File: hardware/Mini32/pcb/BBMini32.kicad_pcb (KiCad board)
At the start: 2 copper layers, 100 x 65 mm, 40 parts, among them J1 POWER, Q1 S8550, Q2 S8050, SW1 SW_Push, SW2 SW_Push, U1 ESP-32_NodeMCU, U2 74HC595, U3 HD44780, U4 MCP3208

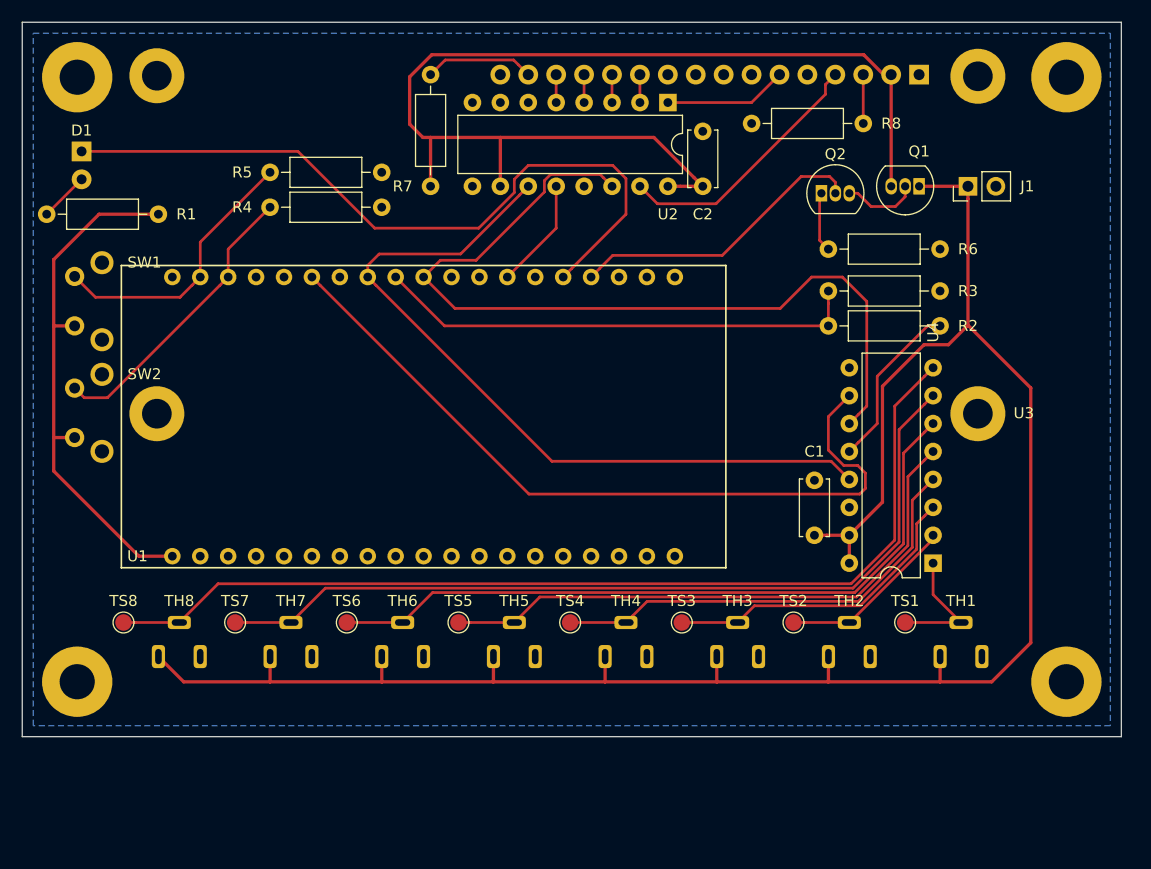
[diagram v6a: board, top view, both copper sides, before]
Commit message: feat: Use transistor to control display
resize and redo PCB

Issue #47
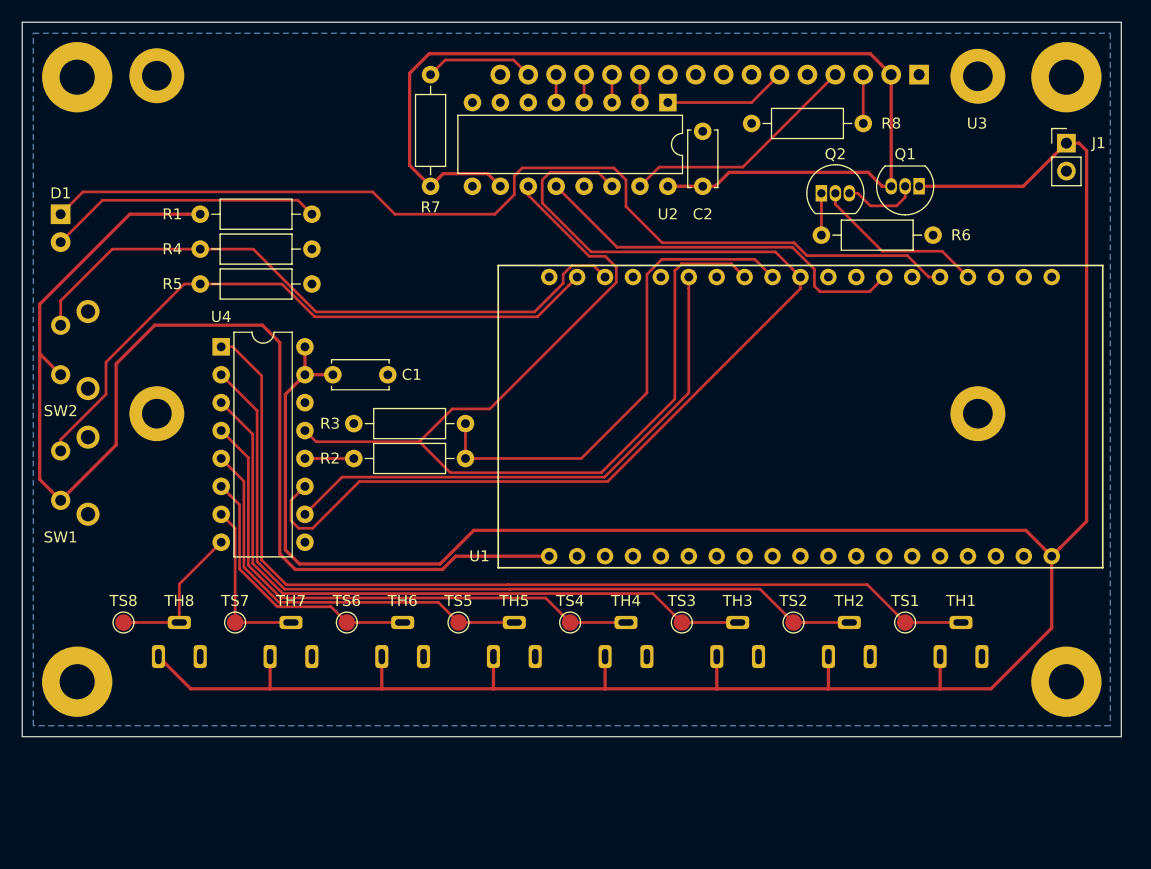
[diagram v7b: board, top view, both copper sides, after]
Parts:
- moved U4 67.7 mm to (38.1, 49.5), turned to 0 degrees
- moved R2 54.7 mm to (50.2, 59.7), turned to 0 degrees
- moved C1 46.2 mm to (48.3, 52.1), turned to 0 degrees
- moved R3 35.2 mm to (60.3, 56.5), turned to 180 degrees
- moved U1 34.3 mm to (90.8, 55.9)
- moved SW1 15.9 mm to (23.5, 59.0)
- moved R5 12.0 mm to (36.2, 43.8)
- moved J1 9.78 mm to (115.0, 31.0), turned to 0 degrees
- moved R4 7.41 mm to (36.2, 40.6)
- moved D1 6.02 mm to (23.5, 37.5)
- moved SW2 5.85 mm to (23.5, 47.6)
- moved R1 3.81 mm to (36.2, 37.5), turned to 0 degrees
- moved R6 1.42 mm to (92.7, 39.4)
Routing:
- net +5V: track 176.8 -> 261.5 mm
- net /SIGNAL8: track 90.4 -> 14.0 mm
- net /SIGNAL1: track 11.5 -> 87.5 mm
- net +3V3: track 48.3 -> 115.7 mm
- net /SIGNAL7: track 78.0 -> 15.4 mm
- net /SIGNAL2: track 16.2 -> 74.5 mm
- net /SIGNAL6: track 65.7 -> 25.1 mm
- net /SIGNAL3: track 28.6 -> 62.2 mm
- net Net-(R5-Pad1): track 25.1 -> 58.3 mm
- net Net-(R4-Pad1): track 26.8 -> 58.7 mm
- net /CS2: track 10.1 -> 35.3 mm
- net /SCLK: track 70.1 -> 93.6 mm
- net Net-(D1-Pad1): track 67.3 -> 90.0 mm
- net Net-(D1-Pad2): track 4.49 -> 25.0 mm
- net /CS1: track 70.1 -> 50.0 mm
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
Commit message: feat: Use transistor to control display
reinsert 5V rail

Issue #47
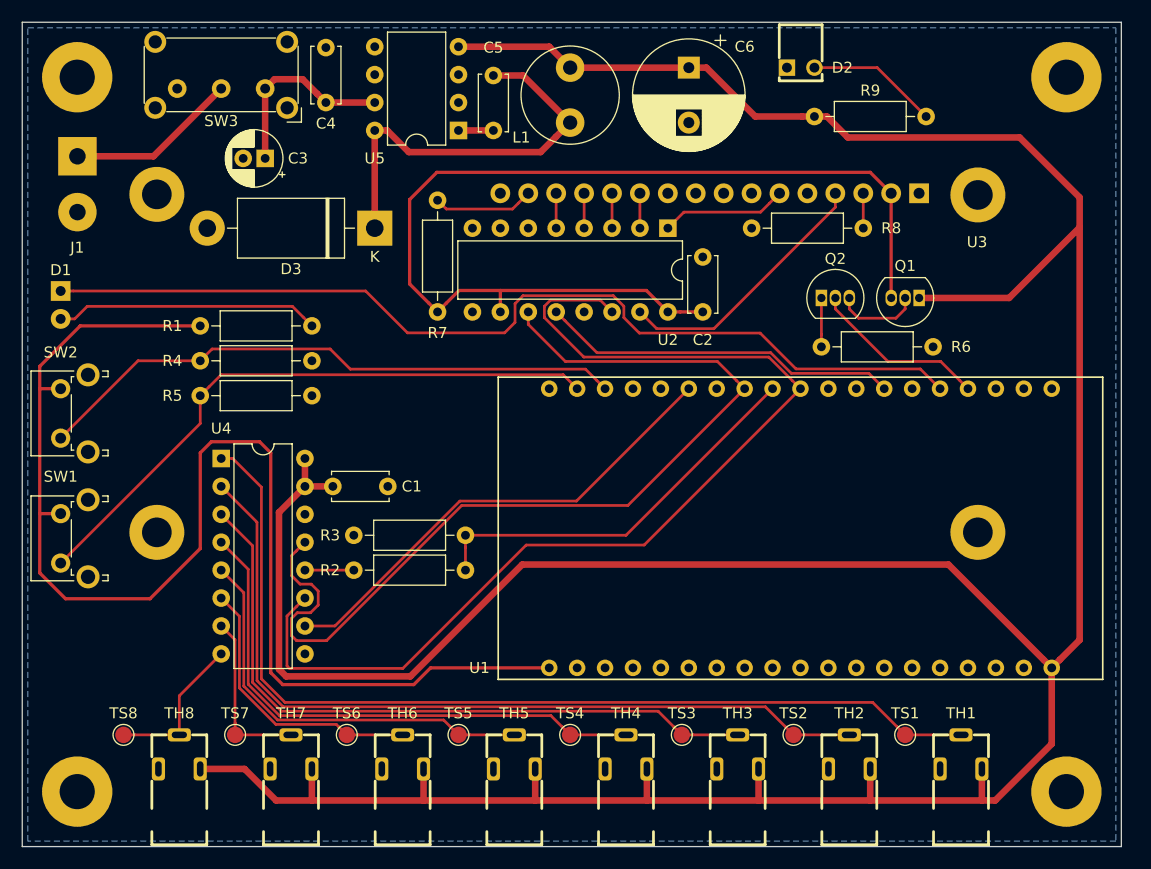
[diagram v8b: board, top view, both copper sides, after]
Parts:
- added C3: 100u, Capacitor_THT:CP_Radial_D5.0mm_P2.00mm, F.Cu at (42.1, 32.4)
- added C4: 100n, Capacitor_THT:C_Disc_D5.0mm_W2.5mm_P5.00mm, F.Cu at (47.6, 27.3)
- added C5: 10n, Capacitor_THT:C_Disc_D5.0mm_W2.5mm_P5.00mm, F.Cu at (62.9, 24.8)
- added C6: 68u, Capacitor_THT:CP_Radial_D10.0mm_P5.00mm, F.Cu at (80.6, 24.1)
- added D2: POWER, VCC:5600F, F.Cu at (90.8, 20.1)
- added D3: 1N5822, Diode_THT:D_DO-201AD_P15.24mm_Horizontal, F.Cu at (52.1, 38.7)
- added L1: 47u, Inductor_THT:L_Radial_D8.7mm_P5.00mm_Fastron_07HCP, F.Cu at (69.8, 29.1)
- added R9: 220, Resistor_THT:R_Axial_DIN0207_L6.3mm_D2.5mm_P10.16mm_Horizontal, F.Cu at (92.1, 28.6)
- added SW3: SW_SPDT, Button_Switch_THT:SW_E-Switch_EG1224_SPDT_Angled, F.Cu at (42.1, 26.0)
- added U5: LM2672M-5.0, Package_DIP:DIP-8_W7.62mm, F.Cu at (59.7, 29.8)
- J1: footprint Connector_PinHeader_2.54mm:PinHeader_1x02_P2.54mm_Vertical -> Connector_Wire:SolderWirePad_1x02_P5.08mm_Drill1.5mm
- SW1, SW2, TH1, TH2, TH3, TH4, TH5, TH6, TH7, TH8: moved to F.Cu
- moved J1 90.0 mm to (25.0, 32.2), turned to 270 degrees
- moved R7 11.4 mm to (57.8, 46.4)
- moved C2 11.4 mm to (81.9, 46.4)
- moved U2 11.4 mm to (78.7, 38.7)
- moved U3 10.8 mm to (69.6, 51.1)
- moved SW2 10.3 mm to (23.5, 57.8), turned to 90 degrees
- moved TH1 10.2 mm to (105.4, 94.8), turned to 180 degrees
- moved TH2 10.2 mm to (95.2, 94.8), turned to 180 degrees
- moved TH3 10.2 mm to (85.1, 94.8), turned to 180 degrees
- moved TH4 10.2 mm to (74.9, 94.8), turned to 180 degrees
- moved TH5 10.2 mm to (64.8, 94.8), turned to 180 degrees
- moved TH6 10.2 mm to (54.6, 94.8), turned to 180 degrees
- moved TH7 10.2 mm to (44.5, 94.8), turned to 180 degrees
- moved TH8 10.2 mm to (34.3, 94.8), turned to 180 degrees
- moved TS1 10.2 mm to (100.3, 84.8)
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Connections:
- J1 pad 1: +5V -> /VPOWER
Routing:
- net +5V: track 261.5 -> 332.5 mm
- net Net-(C5-Pad1): track 0.00 -> 37.4 mm
- net /VIN: track 0.00 -> 17.6 mm
- net /VPOWER: track 0.00 -> 15.6 mm
- net Net-(D2-Pad2): track 0.00 -> 12.0 mm
- net /MISO_5V: track 45.6 -> 36.6 mm
- net /SCLK: track 93.6 -> 86.5 mm
- net /CS1: track 50.0 -> 43.9 mm
- net Net-(R4-Pad1): track 58.7 -> 54.4 mm
- net Net-(C5-Pad2): track 0.00 -> 3.18 mm
- net +3V3: track 115.7 -> 118.6 mm
- net /CS2: track 35.3 -> 32.7 mm
- net /RS: track 22.0 -> 24.3 mm
- net Net-(R5-Pad1): track 58.3 -> 56.1 mm
- net /MOSI: track 95.9 -> 98.1 mm
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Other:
- board size 100 x 65 mm -> 100 x 75 mm
- net class 5V: clearance 0.3 -> 0.2
